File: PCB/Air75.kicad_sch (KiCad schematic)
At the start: 22 parts, among them J1 OLED_128x32, SW1 SW_Push_45deg, SW12 RotaryEncoder_Switch, SW2 SW_Push_45deg, SW3 SW_Push_45deg, SW4 SW_Push_45deg, SW5 SW_Push_45deg, SW6 SW_Push_45deg, SW7 SW_Push_45deg, SW8 SW_Push_45deg, SW9 SW_Push_45deg, U1 XIAO-RP2040-DIP

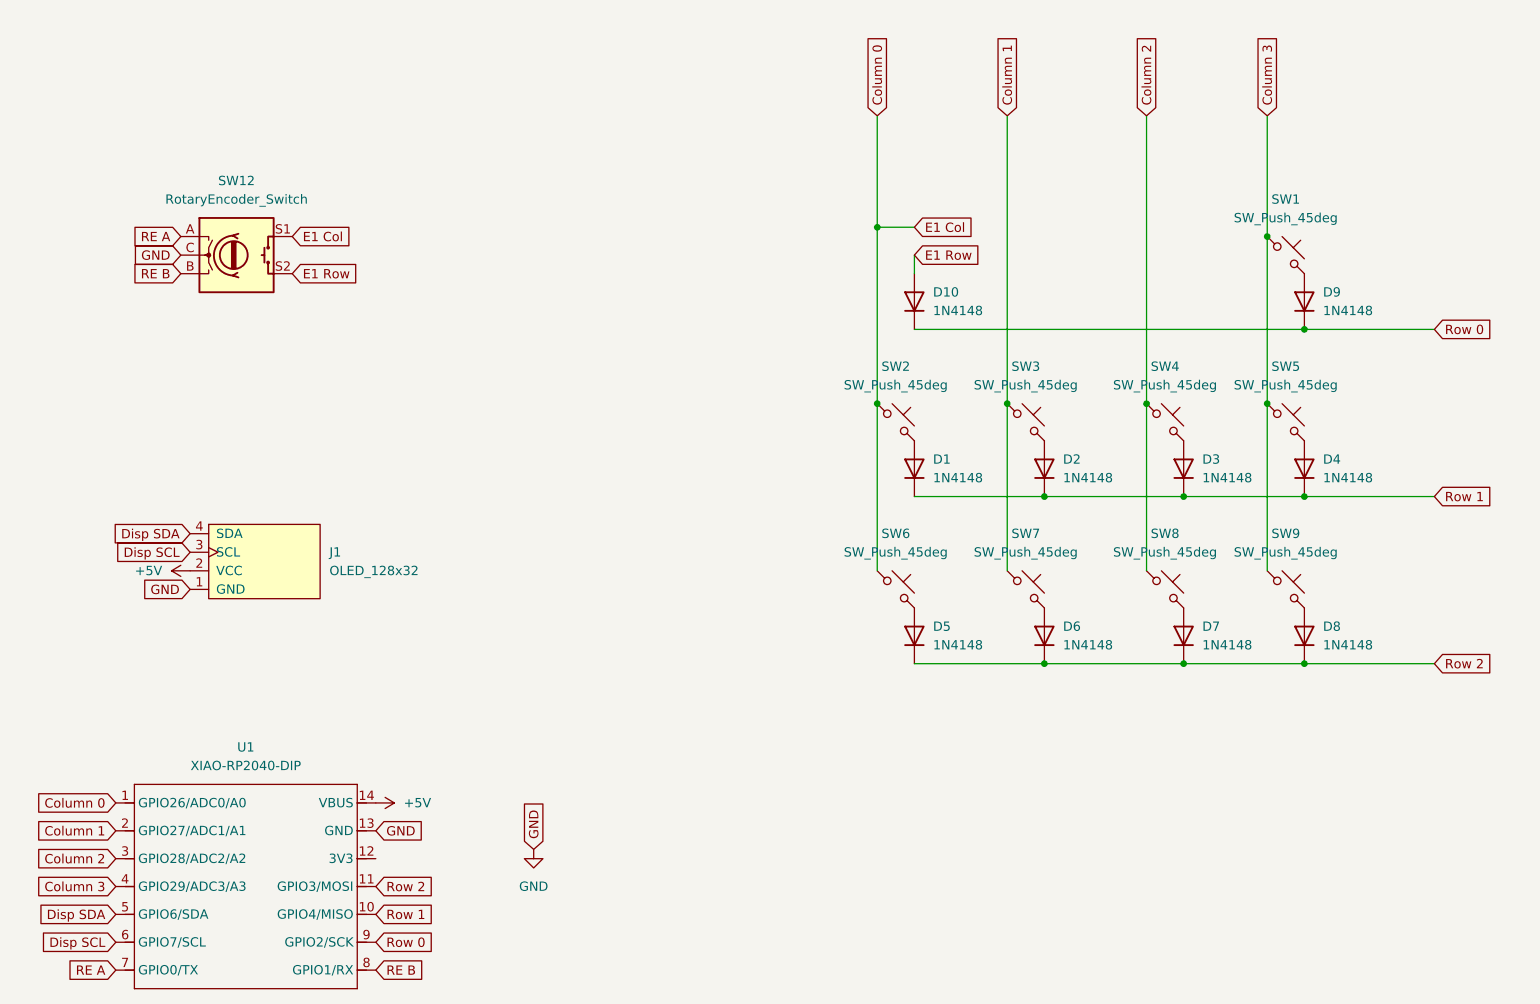
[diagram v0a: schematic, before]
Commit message: fix: remove right angles from pcb
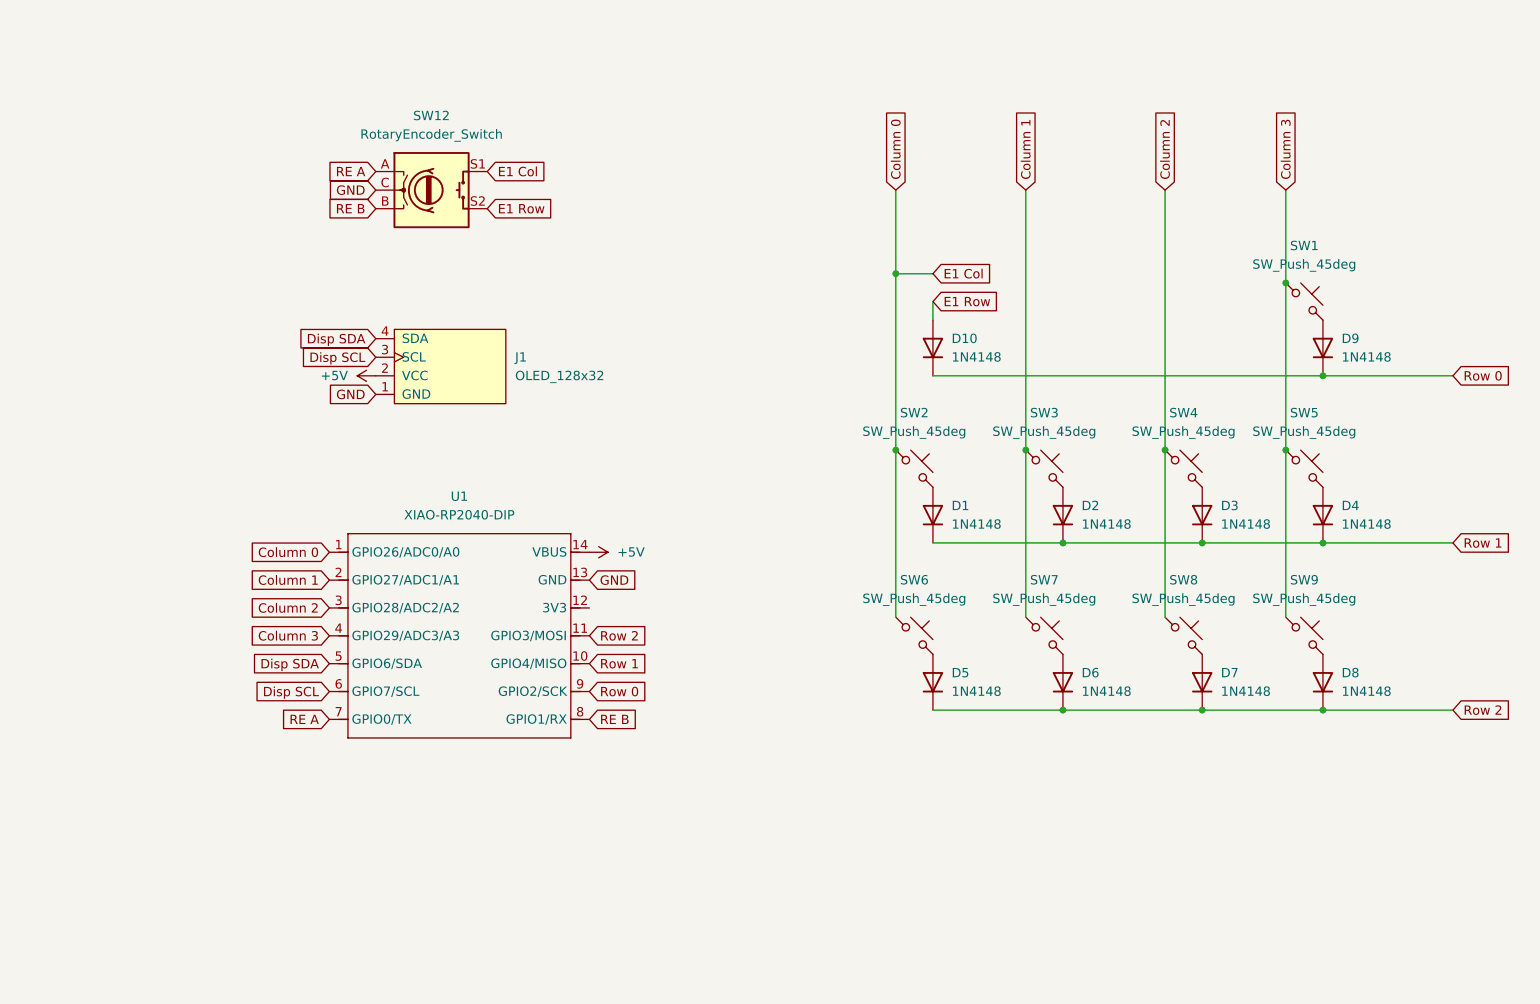
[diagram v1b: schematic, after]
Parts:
- SW1, SW2, SW3, SW4, SW5, SW6, SW7, SW8, SW9: footprint Button_Switch_Keyboard:SW_Cherry_MX_1.00u_PCB -> ScottoKeebs_MX:MX_PCB_1.00u
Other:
- moved on the sheet: D1, D10, D2, D3, D4, D5, D6, D7, D8, D9, J1, SW1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
